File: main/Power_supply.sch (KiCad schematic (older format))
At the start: 32 parts, among them IC2 TPS54294PWP, IC3 TPS54294PWP

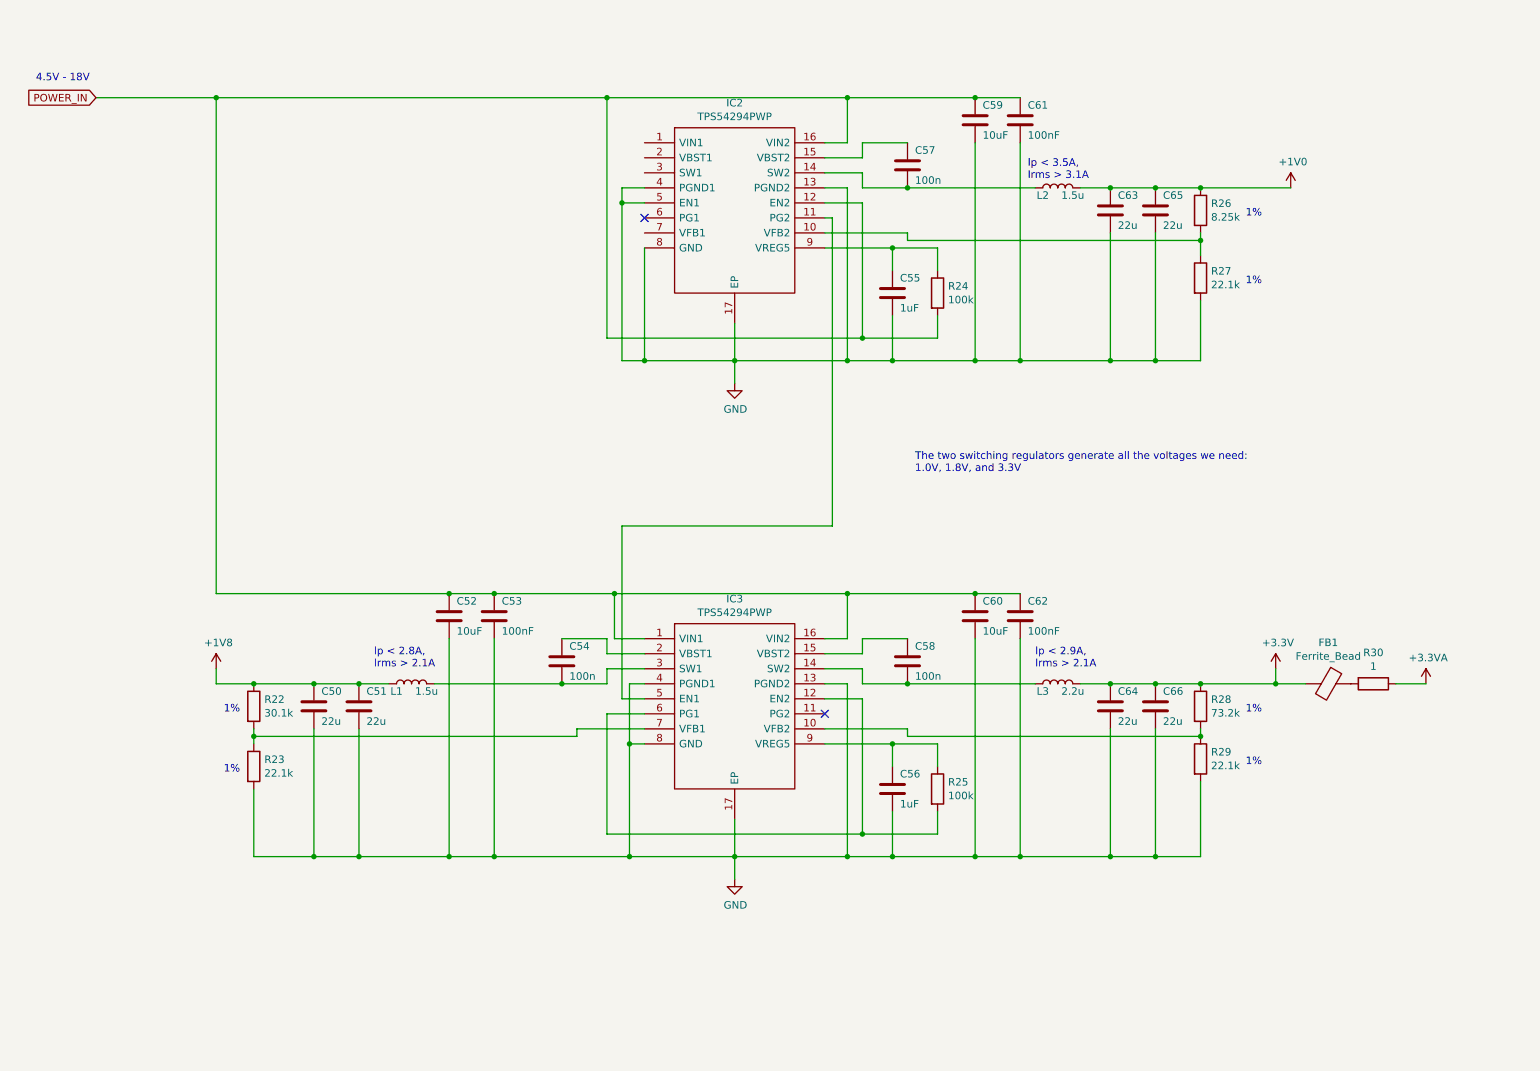
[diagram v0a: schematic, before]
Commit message: Continue wiring of the MCU
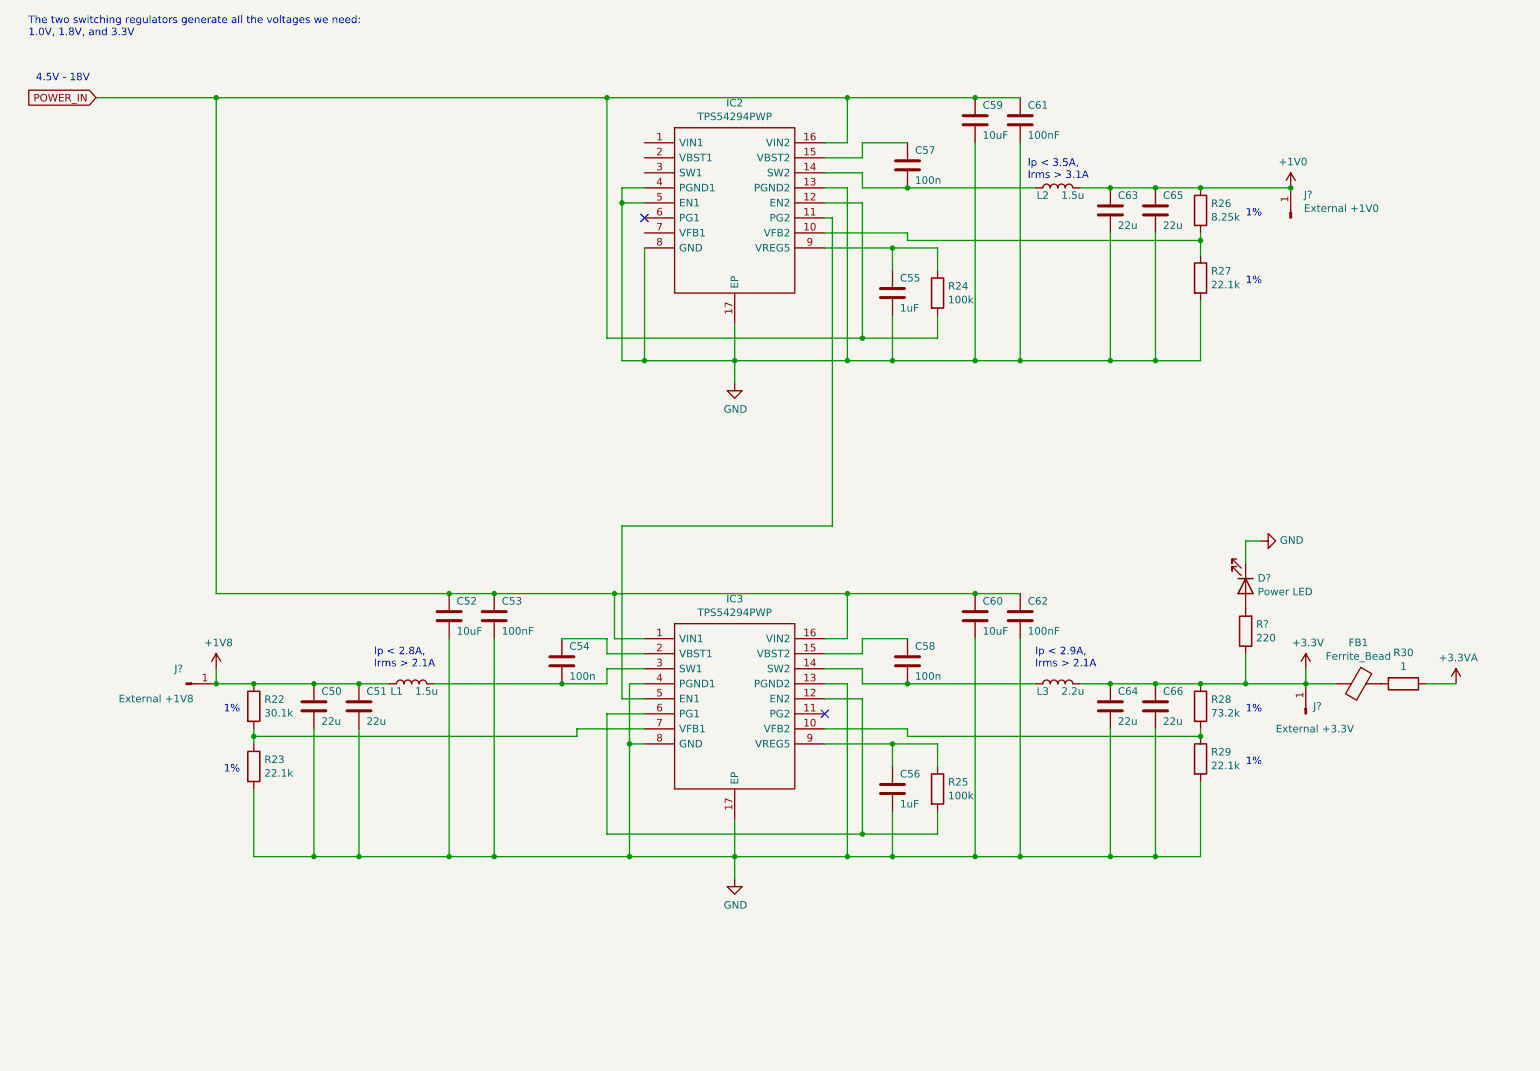
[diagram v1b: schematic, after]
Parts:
- added D?: Power LED, symbol Device:LED
- added J?: External +1V8, symbol Connector:Conn_01x01_Male
- added J?: External +3.3V, symbol Connector:Conn_01x01_Male
- added J?: External +1V0, symbol Connector:Conn_01x01_Male
- added R?: 220, symbol Device:R
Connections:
- net +1V0: now also J?.1 (Pin_1)
- net +1V8: now also J?.1 (Pin_1)
- net +3V3: now also J?.1 (Pin_1), R?.1
- net GND: now also D?.1 (K)
- new net: D?.2 (A), R?.2
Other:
- moved on the sheet: FB1, R30
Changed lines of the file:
@@
 $Descr A4 11693 8268
 encoding utf-8
-Sheet 7 7
+Sheet 6 7
 Title ""
 Date ""
@@
 	7950 6350 8250 6350
 Connection ~ 8250 6350
-Wire Wire Line
-	8550 5200 9050 5200
-Connection ~ 8550 5200
 $Comp
 L power:+3.3V #PWR0160
 U 1 1 614E8685
-P 9050 5100
-F 0 "#PWR0160" H 9050 4950 50  0001 C CNN
-F 1 "+3.3V" H 9065 5273 50  0000 C CNN
-F 2 "" H 9050 5100 50  0001 C CNN
-F 3 "" H 9050 5100 50  0001 C CNN
-	1    9050 5100
-	1    0    0    -1
-$EndComp
-Connection ~ 9050 5200
-Wire Wire Line
-	9050 5200 9250 5200
+P 9250 5100
+F 0 "#PWR0160" H 9250 4950 50  0001 C CNN
+F 1 "+3.3V" H 9265 5273 50  0000 C CNN
+F 2 "" H 9250 5100 50  0001 C CNN
+F 3 "" H 9250 5100 50  0001 C CNN
+	1    9250 5100
+	1    0    0    -1
+$EndComp
+Wire Wire Line
+	9250 5200 9450 5200
 $Comp
 L Device:Ferrite_Bead FB1
 U 1 1 614E921D
-P 9400 5200
-F 0 "FB1" V 9126 5200 50  0000 C CNN
-F 1 "Ferrite_Bead" V 9217 5200 50  0000 C CNN
-F 2 "" V 9330 5200 50  0001 C CNN
-F 3 "~" H 9400 5200 50  0001 C CNN
-	1    9400 5200
+P 9600 5200
+F 0 "FB1" V 9326 5200 50  0000 C CNN
+F 1 "Ferrite_Bead" V 9417 5200 50  0000 C CNN
+F 2 "" V 9530 5200 50  0001 C CNN
+F 3 "~" H 9600 5200 50  0001 C CNN
+	1    9600 5200
 	0    1    1    0
 $EndComp
@@
 L Device:R R30
 U 1 1 614E9A01
-P 9700 5200
-F 0 "R30" V 9493 5200 50  0000 C CNN
-F 1 "1" V 9584 5200 50  0000 C CNN
-F 2 "" V 9630 5200 50  0001 C CNN
-F 3 "~" H 9700 5200 50  0001 C CNN
-	1    9700 5200
+P 9900 5200
+F 0 "R30" V 9693 5200 50  0000 C CNN
+F 1 "1" V 9784 5200 50  0000 C CNN
+F 2 "" V 9830 5200 50  0001 C CNN
+F 3 "~" H 9900 5200 50  0001 C CNN
+	1    9900 5200
 	0    1    1    0
 $EndComp
@@
 L power:+3.3VA #PWR0161
 U 1 1 614EA42D
-P 10050 5200
-F 0 "#PWR0161" H 10050 5050 50  0001 C CNN
-F 1 "+3.3VA" H 10065 5373 50  0000 C CNN
-F 2 "" H 10050 5200 50  0001 C CNN
-F 3 "" H 10050 5200 50  0001 C CNN
-	1    10050 5200
-	1    0    0    -1
-$EndComp
-Wire Wire Line
-	9850 5200 10050 5200
+P 10250 5200
+F 0 "#PWR0161" H 10250 5050 50  0001 C CNN
+F 1 "+3.3VA" H 10265 5373 50  0000 C CNN
+F 2 "" H 10250 5200 50  0001 C CNN
+F 3 "" H 10250 5200 50  0001 C CNN
+	1    10250 5200
+	1    0    0    -1
+$EndComp
+Wire Wire Line
+	10050 5200 10250 5200
 Wire Wire Line
 	8550 5850 8550 6350
@@
 Connection ~ 4700 2000
 Wire Wire Line
-	9050 5100 9050 5200
+	9250 5100 9250 5200
 Wire Wire Line
 	2250 5500 2250 5550
@@
 Text Notes 2050 5800 0    50   ~ 0
 1%
-Text Notes 6650 3800 0    50   ~ 0
+Text Notes 750  900  0    50   ~ 0
 The two switching regulators generate all the voltages we need:\n1.0V, 1.8V, and 3.3V
+Connection ~ 8550 5200
+$Comp
+L Device:LED D?
+U 1 1 61865DA3
+P 8850 4550
+F 0 "D?" V 8797 4630 50  0000 L CNN
+F 1 "Power LED" V 8888 4630 50  0000 L CNN
+F 2 "" H 8850 4550 50  0001 C CNN
+F 3 "~" H 8850 4550 50  0001 C CNN
+	1    8850 4550
+	0    1    1    0
+$EndComp
+Wire Wire Line
+	8550 5200 8850 5200
+Wire Wire Line
+	8850 5000 8850 5200
+$Comp
+L Device:R R?
+U 1 1 61866DAC
+P 8850 4850
+F 0 "R?" H 8780 4804 50  0000 R CNN
+F 1 "220" H 8780 4895 50  0000 R CNN
+F 2 "" V 8780 4850 50  0001 C CNN
+F 3 "~" H 8850 4850 50  0001 C CNN
+	1    8850 4850
+	-1   0    0    1
+$EndComp
+$Comp
+L power:GND #PWR?
+U 1 1 61877ACD
+P 8950 4250
+F 0 "#PWR?" H 8950 4000 50  0001 C CNN
+F 1 "GND" V 8955 4122 50  0000 R CNN
+F 2 "" H 8950 4250 50  0001 C CNN
+F 3 "" H 8950 4250 50  0001 C CNN
+	1    8950 4250
+	0    -1   -1   0
+$EndComp
+Wire Wire Line
+	8850 4400 8850 4250
+Wire Wire Line
+	8850 4250 8950 4250
+Wire Wire Line
+	8850 5200 9250 5200
+Connection ~ 8850 5200
+Connection ~ 9250 5200
+$Comp
+L Connector:Conn_01x01_Male J?
+U 1 1 6189543E
+P 1800 5200
+F 0 "J?" H 1750 5300 50  0000 C CNN
+F 1 "External +1V8" H 1600 5100 50  0000 C CNN
+F 2 "" H 1800 5200 50  0001 C CNN
+F 3 "~" H 1800 5200 50  0001 C CNN
+	1    1800 5200
+	1    0    0    -1
+$EndComp
+Connection ~ 2000 5200
+$Comp
+L Connector:Conn_01x01_Male J?
+U 1 1 61895F3D
+P 9250 5400
+F 0 "J?" V 9300 5350 50  0000 R CNN
+F 1 "External +3.3V" V 9150 5600 50  0000 R CNN
+F 2 "" H 9250 5400 50  0001 C CNN
+F 3 "~" H 9250 5400 50  0001 C CNN
+	1    9250 5400
+	0    -1   -1   0
+$EndComp
+$Comp
+L Connector:Conn_01x01_Male J?
+U 1 1 61896E72
+P 9150 2100
+F 0 "J?" V 9304 2012 50  0000 R CNN
+F 1 "External +1V0" V 9213 2012 50  0000 R CNN
+F 2 "" H 9150 2100 50  0001 C CNN
+F 3 "~" H 9150 2100 50  0001 C CNN
+	1    9150 2100
+	0    -1   -1   0
+$EndComp
+Connection ~ 9150 1900
 $EndSCHEMATC

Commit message: Be consistent with capacitor values (always use F)
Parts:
- C50, C51, C63, C64, C65, C66: value 22u -> 22uF
- C54, C57, C58: value 100n -> 100nF
- gave numbers to parts that had none: 5
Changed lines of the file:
@@
 P 6600 5050
 F 0 "C58" H 6650 5150 50  0000 L CNN
-F 1 "100n" H 6650 4950 50  0000 L CNN
+F 1 "100nF" H 6650 4950 50  0000 L CNN
 F 2 "" H 6638 4900 50  0001 C CNN
 F 3 "~" H 6600 5050 50  0001 C CNN
@@
 P 4300 5050
 F 0 "C54" H 4350 5150 50  0000 L CNN
-F 1 "100n" H 4350 4950 50  0000 L CNN
+F 1 "100nF" H 4350 4950 50  0000 L CNN
 F 2 "" H 4338 4900 50  0001 C CNN
 F 3 "~" H 4300 5050 50  0001 C CNN
@@
 P 2950 5350
 F 0 "C51" H 3000 5450 50  0000 L CNN
-F 1 "22u" H 3000 5250 50  0000 L CNN
+F 1 "22uF" H 3000 5250 50  0000 L CNN
 F 2 "" H 2988 5200 50  0001 C CNN
 F 3 "~" H 2950 5350 50  0001 C CNN
@@
 P 2650 5350
 F 0 "C50" H 2700 5450 50  0000 L CNN
-F 1 "22u" H 2700 5250 50  0000 L CNN
+F 1 "22uF" H 2700 5250 50  0000 L CNN
 F 2 "" H 2688 5200 50  0001 C CNN
 F 3 "~" H 2650 5350 50  0001 C CNN
@@
 P 8250 5350
 F 0 "C66" H 8300 5450 50  0000 L CNN
-F 1 "22u" H 8300 5250 50  0000 L CNN
+F 1 "22uF" H 8300 5250 50  0000 L CNN
 F 2 "" H 8288 5200 50  0001 C CNN
 F 3 "~" H 8250 5350 50  0001 C CNN
@@
 P 7950 5350
 F 0 "C64" H 8000 5450 50  0000 L CNN
-F 1 "22u" H 8000 5250 50  0000 L CNN
+F 1 "22uF" H 8000 5250 50  0000 L CNN
 F 2 "" H 7988 5200 50  0001 C CNN
 F 3 "~" H 7950 5350 50  0001 C CNN
@@
 P 6600 1750
 F 0 "C57" H 6650 1850 50  0000 L CNN
-F 1 "100n" H 6650 1650 50  0000 L CNN
+F 1 "100nF" H 6650 1650 50  0000 L CNN
 F 2 "" H 6638 1600 50  0001 C CNN
 F 3 "~" H 6600 1750 50  0001 C CNN
@@
 P 8250 2050
 F 0 "C65" H 8300 2150 50  0000 L CNN
-F 1 "22u" H 8300 1950 50  0000 L CNN
+F 1 "22uF" H 8300 1950 50  0000 L CNN
 F 2 "" H 8288 1900 50  0001 C CNN
 F 3 "~" H 8250 2050 50  0001 C CNN
@@
 P 7950 2050
 F 0 "C63" H 8000 2150 50  0000 L CNN
-F 1 "22u" H 8000 1950 50  0000 L CNN
+F 1 "22uF" H 8000 1950 50  0000 L CNN
 F 2 "" H 7988 1900 50  0001 C CNN
 F 3 "~" H 7950 2050 50  0001 C CNN
@@
 Connection ~ 8550 5200
 $Comp
-L Device:LED D?
+L Device:LED D6
 U 1 1 61865DA3
 P 8850 4550
-F 0 "D?" V 8797 4630 50  0000 L CNN
+F 0 "D6" V 8797 4630 50  0000 L CNN
 F 1 "Power LED" V 8888 4630 50  0000 L CNN
 F 2 "" H 8850 4550 50  0001 C CNN
@@
 	8850 5000 8850 5200
 $Comp
-L Device:R R?
+L Device:R R35
 U 1 1 61866DAC
 P 8850 4850
-F 0 "R?" H 8780 4804 50  0000 R CNN
+F 0 "R35" H 8780 4804 50  0000 R CNN
 F 1 "220" H 8780 4895 50  0000 R CNN
 F 2 "" V 8780 4850 50  0001 C CNN
@@
 $EndComp
 $Comp
-L power:GND #PWR?
+L power:GND #PWR0165
 U 1 1 61877ACD
 P 8950 4250
-F 0 "#PWR?" H 8950 4000 50  0001 C CNN
+F 0 "#PWR0165" H 8950 4000 50  0001 C CNN
 F 1 "GND" V 8955 4122 50  0000 R CNN
 F 2 "" H 8950 4250 50  0001 C CNN
@@
 Connection ~ 9250 5200
 $Comp
-L Connector:Conn_01x01_Male J?
+L Connector:Conn_01x01_Male J7
 U 1 1 6189543E
 P 1800 5200
-F 0 "J?" H 1750 5300 50  0000 C CNN
+F 0 "J7" H 1750 5300 50  0000 C CNN
 F 1 "External +1V8" H 1600 5100 50  0000 C CNN
 F 2 "" H 1800 5200 50  0001 C CNN
@@
 Connection ~ 2000 5200
 $Comp
-L Connector:Conn_01x01_Male J?
+L Connector:Conn_01x01_Male J9
 U 1 1 61895F3D
 P 9250 5400
-F 0 "J?" V 9300 5350 50  0000 R CNN
+F 0 "J9" V 9300 5350 50  0000 R CNN
 F 1 "External +3.3V" V 9150 5600 50  0000 R CNN
 F 2 "" H 9250 5400 50  0001 C CNN
@@
 $EndComp
 $Comp
-L Connector:Conn_01x01_Male J?
+L Connector:Conn_01x01_Male J8
 U 1 1 61896E72
 P 9150 2100
-F 0 "J?" V 9304 2012 50  0000 R CNN
+F 0 "J8" V 9304 2012 50  0000 R CNN
 F 1 "External +1V0" V 9213 2012 50  0000 R CNN
 F 2 "" H 9150 2100 50  0001 C CNN

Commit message: FPGA connections, DAC linear regulator removed, DAC I2S breakout
Connected the SPI, I2S and GPIO to some (mostly) arbitrary pins. Notably
the SPI clock has to be connected to a clock pin on the FPGA.

The linear regulator is (hopefully) not needed for the DAC as we already
have a separate analog +3.3V created by the switching regulators.

The I2S wires to the DAC are now connected to the FPGA as well as
breakout pins over 0 ohm resistors, in case we need to connect to an
external FPGA.
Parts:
- added J?: Barrel_Jack, symbol Connector:Barrel_Jack
- L1, L2: value 1.5u -> 1.5uH
- L3: value 2.2u -> 2.2uH
- R26: value 8.25k -> 6.81k
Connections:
- net POWER_IN is gone; now on an unnamed net: C52.1, C53.1, C59.1, C60.1, C61.1, C62.1, IC2.12 (EN2), IC2.16 (VIN2), IC3.1 (VIN1), IC3.16 (VIN2), R24.2
- net GND: now also J?.2
- net at IC2.1 (VIN1): now also J?.1
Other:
- note added: "12V"
- note removed: "4.5V - 18V"
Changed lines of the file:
@@
 P 3300 5200
 F 0 "L1" V 3250 5300 50  0000 C CNN
-F 1 "1.5u" V 3250 5100 50  0000 C CNN
+F 1 "1.5uH" V 3250 5100 50  0000 C CNN
 F 2 "" H 3300 5200 50  0001 C CNN
 F 3 "~" H 3300 5200 50  0001 C CNN
@@
 P 7600 5200
 F 0 "L3" V 7550 5300 50  0000 C CNN
-F 1 "2.2u" V 7550 5100 50  0000 C CNN
+F 1 "2.2uH" V 7550 5100 50  0000 C CNN
 F 2 "" H 7600 5200 50  0001 C CNN
 F 3 "~" H 7600 5200 50  0001 C CNN
@@
 Wire Wire Line
 	8250 6350 8550 6350
-Text GLabel 1200 1300 0    50   Input ~ 0
-POWER_IN
-Text Notes 800  1200 0    50   ~ 0
-4.5V - 18V
+Text Notes 850  1650 0    50   ~ 0
+12V
 Wire Wire Line
 	1200 1300 2000 1300
@@
 P 7600 1900
 F 0 "L2" V 7550 2000 50  0000 C CNN
-F 1 "1.5u" V 7550 1800 50  0000 C CNN
+F 1 "1.5uH" V 7550 1800 50  0000 C CNN
 F 2 "" H 7600 1900 50  0001 C CNN
 F 3 "~" H 7600 1900 50  0001 C CNN
@@
 P 8550 2050
 F 0 "R26" H 8620 2096 50  0000 L CNN
-F 1 "8.25k" H 8620 2005 50  0000 L CNN
+F 1 "6.81k" H 8620 2005 50  0000 L CNN
 F 2 "" V 8480 2050 50  0001 C CNN
 F 3 "~" H 8550 2050 50  0001 C CNN
@@
 Connection ~ 4600 1300
 Wire Wire Line
-	4600 1300 6200 1300
+	4600 1300 4850 1300
 Wire Wire Line
 	4850 2000 4700 2000
@@
 $EndComp
 Connection ~ 9150 1900
+$Comp
+L Connector:Barrel_Jack J?
+U 1 1 614B1C0A
+P 900 1400
+F 0 "J?" H 957 1725 50  0000 C CNN
+F 1 "Barrel_Jack" H 957 1634 50  0000 C CNN
+F 2 "" H 950 1360 50  0001 C CNN
+F 3 "~" H 950 1360 50  0001 C CNN
+	1    900  1400
+	1    0    0    -1
+$EndComp
+$Comp
+L power:GND #PWR?
+U 1 1 614B2BBB
+P 1400 1700
+F 0 "#PWR?" H 1400 1450 50  0001 C CNN
+F 1 "GND" H 1405 1527 50  0000 C CNN
+F 2 "" H 1400 1700 50  0001 C CNN
+F 3 "" H 1400 1700 50  0001 C CNN
+	1    1400 1700
+	1    0    0    -1
+$EndComp
+Wire Wire Line
+	1200 1500 1400 1500
+Wire Wire Line
+	1400 1500 1400 1700
+Wire Wire Line
+	4850 1600 4850 1300
+Connection ~ 4850 1300
+Wire Wire Line
+	4850 1300 6200 1300
 $EndSCHEMATC
